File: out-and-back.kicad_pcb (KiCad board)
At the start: 2 copper layers, 40.6 x 30.5 mm, 4 parts, among them J1 430450400, J2 430450400, J3 Conn_01x04

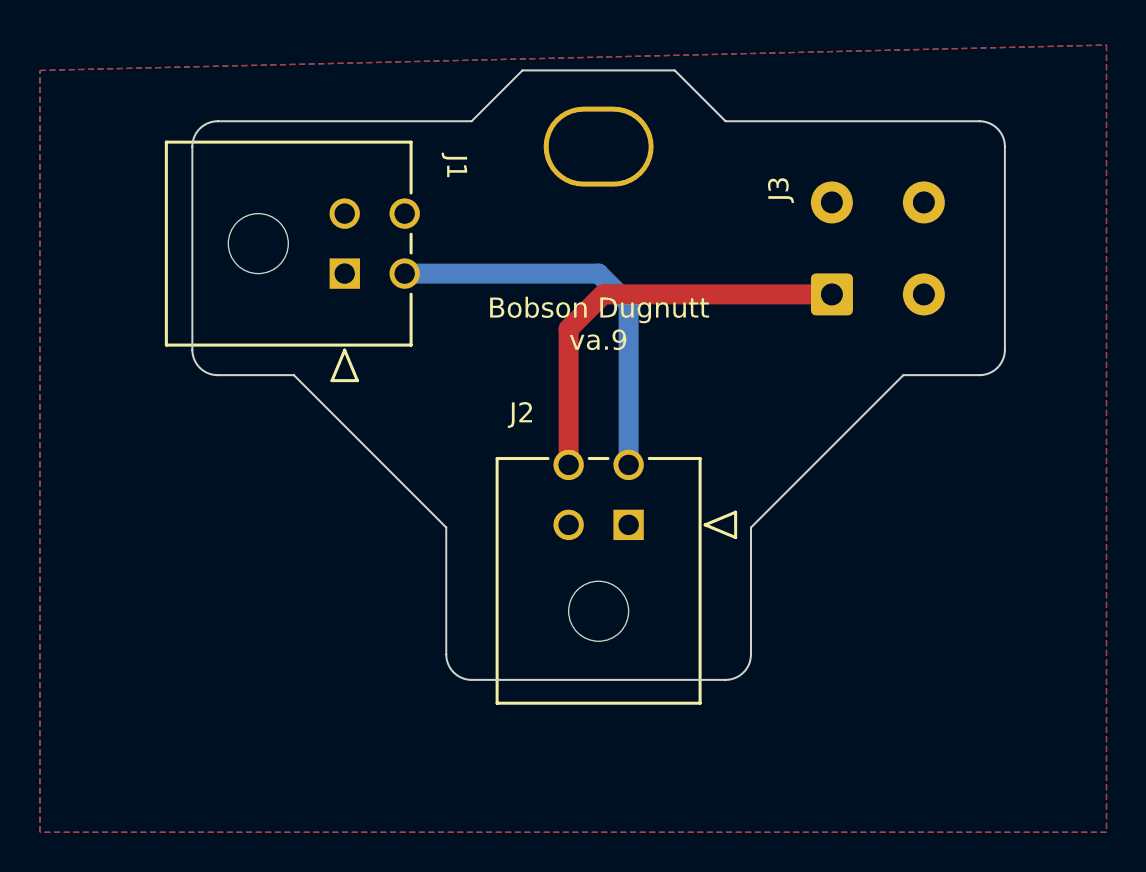
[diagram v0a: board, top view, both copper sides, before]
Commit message: Widen holes
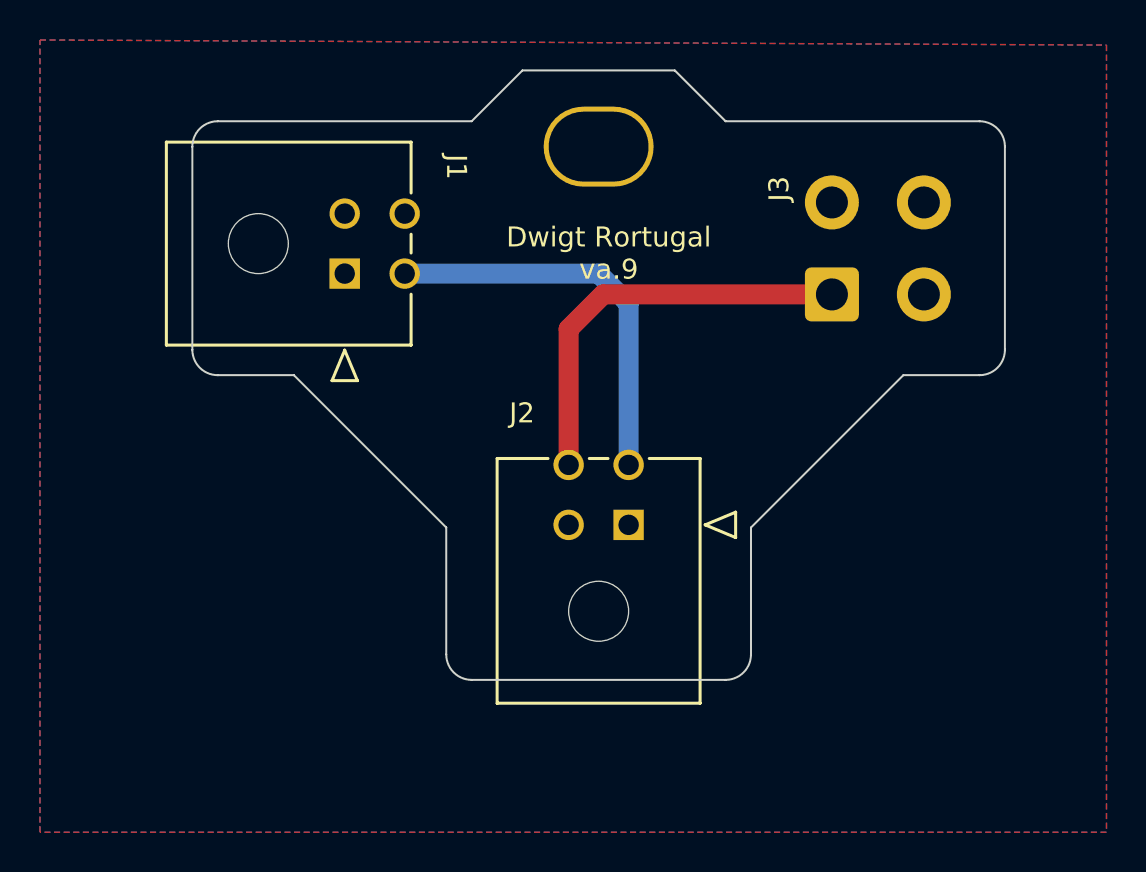
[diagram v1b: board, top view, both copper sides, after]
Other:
- board text added: "DATA IN"
- board text added: "DATA OUT"
- board text added: "Dwigt Rortugal va.9"
- board text added: "OUT AND BACK"
- board text removed: "Bobson Dugnutt va.9"
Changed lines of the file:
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@@
       (layerselection 0x00010fc_ffffffff)
       (disableapertmacros false)
-      (usegerberextensions false)
+      (usegerberextensions true)
       (usegerberattributes true)
       (usegerberadvancedattributes true)
-      (creategerberjobfile true)
+      (creategerberjobfile false)
       (svguseinch false)
       (svgprecision 6)
@@
       (psa4output false)
       (plotreference true)
-      (plotvalue true)
+      (plotvalue false)
       (plotinvisibletext false)
       (sketchpadsonfab false)
-      (subtractmaskfromsilk false)
+      (subtractmaskfromsilk true)
       (outputformat 1)
       (mirror false)
-      (drillshape 1)
+      (drillshape 0)
       (scaleselection 1)
-      (outputdirectory "")
+      (outputdirectory "/home/spidergod/Downloads/jlc_outputs/")
     )
   )
@@
     (fp_circle (center 4.6 0) (end 5.65 0) (layer "F.Fab") (width 0.1) (fill none))
     (fp_circle (center 0 4.572) (end 1.05 4.572) (layer "F.Fab") (width 0.1) (fill none))
-    (pad "1" thru_hole circle (at 0 4.6 90) (size 2.1 2.1) (drill 1.1) (layers *.Cu *.Mask)
+    (pad "1" thru_hole circle (at 0 4.6 90) (size 2.7 2.7) (drill 1.6) (layers *.Cu *.Mask)
       (net 1 "/VCC") (pinfunction "Pin_1") (pintype "passive"))
-    (pad "2" thru_hole circle (at 4.6 4.6 90) (size 2.1 2.1) (drill 1.1) (layers *.Cu *.Mask)
+    (pad "2" thru_hole circle (at 4.6 4.6 90) (size 2.7 2.7) (drill 1.6) (layers *.Cu *.Mask)
       (net 2 "/GND") (pinfunction "Pin_2") (pintype "passive"))
-    (pad "3" thru_hole roundrect (at 0 0 90) (size 2.1 2.1) (drill 1.1) (layers *.Cu *.Mask) (roundrect_rratio 0.119048)
+    (pad "3" thru_hole roundrect (at 0 0 90) (size 2.7 2.7) (drill 1.6) (layers *.Cu *.Mask) (roundrect_rratio 0.1190481481)
       (net 4 "/DATA_OUT") (pinfunction "Pin_3") (pintype "passive"))
-    (pad "4" thru_hole circle (at 4.6 0 90) (size 2.1 2.1) (drill 1.1) (layers *.Cu *.Mask)
+    (pad "4" thru_hole circle (at 4.6 0 90) (size 2.7 2.7) (drill 1.6) (layers *.Cu *.Mask)
       (net 2 "/GND") (pinfunction "Pin_4") (pintype "passive"))
     (model "${KICAD6_3DMODEL_DIR}/Connector_Wire.3dshapes/SolderWire-0.5sqmm_1x04_P4.6mm_D0.9mm_OD2.1mm.wrl"
@@
   (gr_line (start 135.89 45.72) (end 138.43 48.26) (layer "Edge.Cuts") (width 0.1))
   (gr_line (start 152.4 59.69) (end 152.4 49.53) (layer "Edge.Cuts") (width 0.1))
-  (gr_text "Bobson Dugnutt\nva.9" (at 132.08 58.42) (layer "F.SilkS")
+  (gr_text "OUT AND BACK" (at 132.08 62.484) (layer "B.SilkS")
+    (effects (font (size 1 1) (thickness 0.15)) (justify mirror))
+  )
+  (gr_text "DATA IN" (at 125.984 54.864 270) (layer "B.SilkS")
+    (effects (font (size 1 1) (thickness 0.15)) (justify mirror))
+  )
+  (gr_text "DATA OUT" (at 140.208 54.864 90) (layer "B.SilkS")
+    (effects (font (size 1 1) (thickness 0.15)) (justify mirror))
+  )
+  (gr_text "Dwigt Rortugal\nva.9" (at 132.588 54.864) (layer "F.SilkS")
     (effects (font (size 1 1) (thickness 0.15)))
   )
@@
     (connect_pads (clearance 0.508))
     (min_thickness 0.254) (filled_areas_thickness no)
-    (fill yes (thermal_gap 0.508) (thermal_bridge_width 0.508))
+    (fill (thermal_gap 0.508) (thermal_bridge_width 0.508))
     (polygon
       (pts
         (xy 157.48 83.82)
         (xy 104.14 83.82)
-        (xy 104.14 45.72)
+        (xy 104.14 44.196)
         (xy 157.48 44.45)
       )
@@
     (connect_pads (clearance 0.508))
     (min_thickness 0.254) (filled_areas_thickness no)
-    (fill yes (thermal_gap 0.508) (thermal_bridge_width 0.508))
+    (fill (thermal_gap 0.508) (thermal_bridge_width 0.508))
     (polygon
       (pts
         (xy 157.48 83.82)
         (xy 104.14 83.82)
-        (xy 104.14 45.72)
+        (xy 104.14 44.196)
         (xy 157.48 44.45)
       )

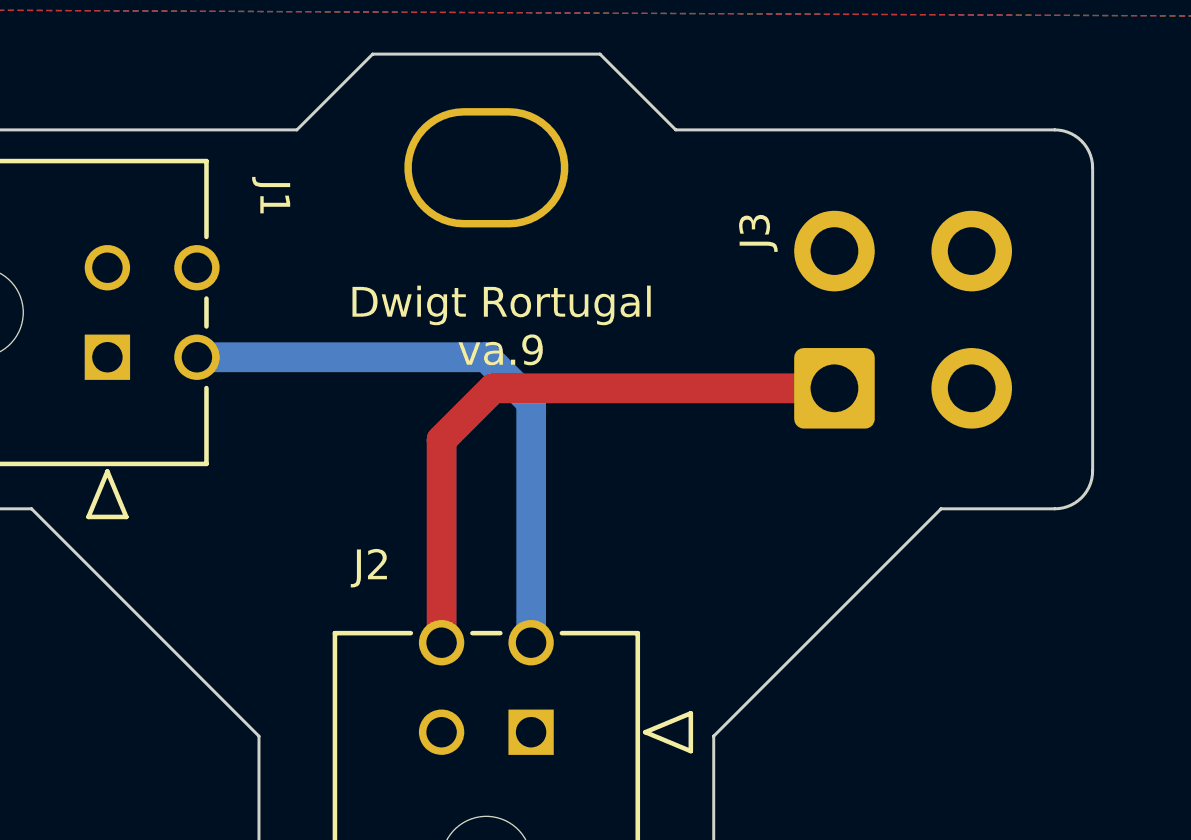
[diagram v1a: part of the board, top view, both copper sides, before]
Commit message: Fix fill and routing errors
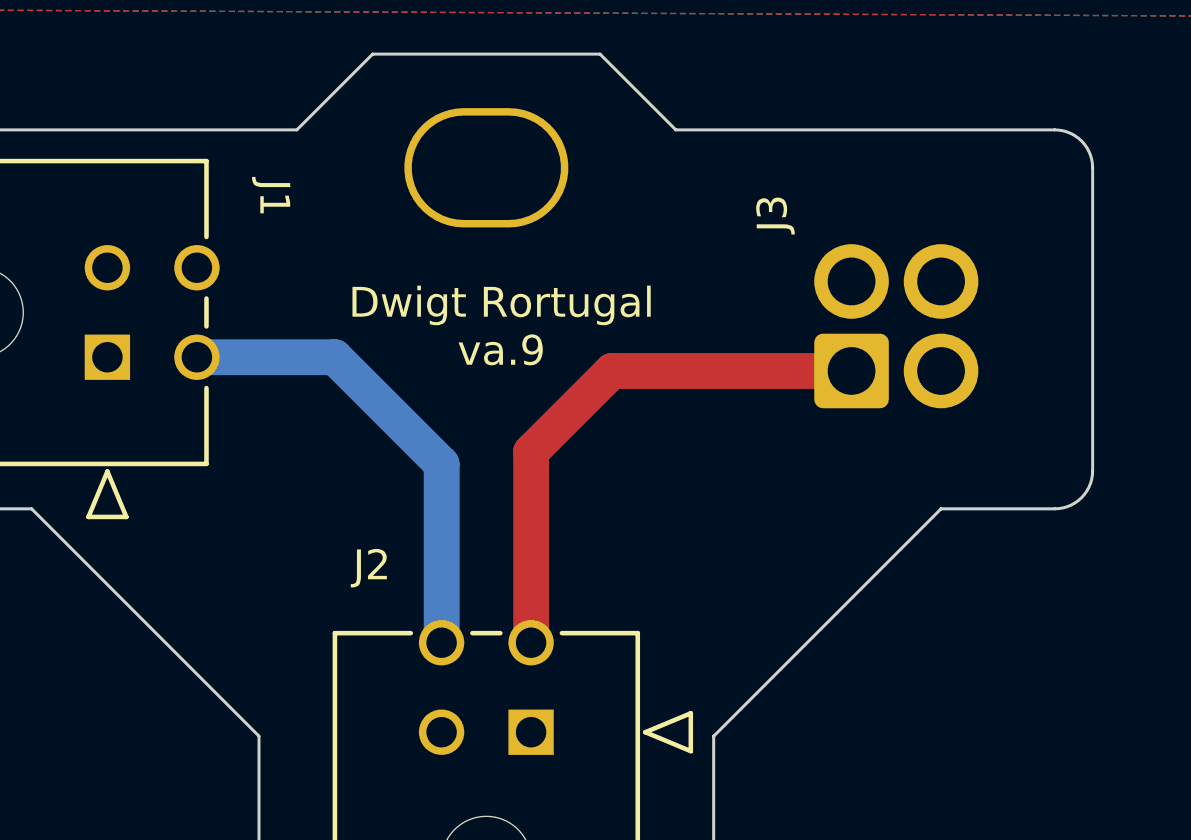
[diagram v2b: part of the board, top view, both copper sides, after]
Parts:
- moved J3 0.82 mm to (144.3, 56.3)
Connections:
- J2 pad 3: /DATA_IN -> /DATA_OUT
- J2 pad 4: /DATA_OUT -> /DATA_IN
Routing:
- net /DATA_IN: track 19.9 -> 15.7 mm
- net /DATA_OUT: track 20.7 -> 18.3 mm
